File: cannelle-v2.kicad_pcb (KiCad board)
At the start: 2 copper layers, 62 parts, among them P1 USB_OTG, U6 ICE40HX1K

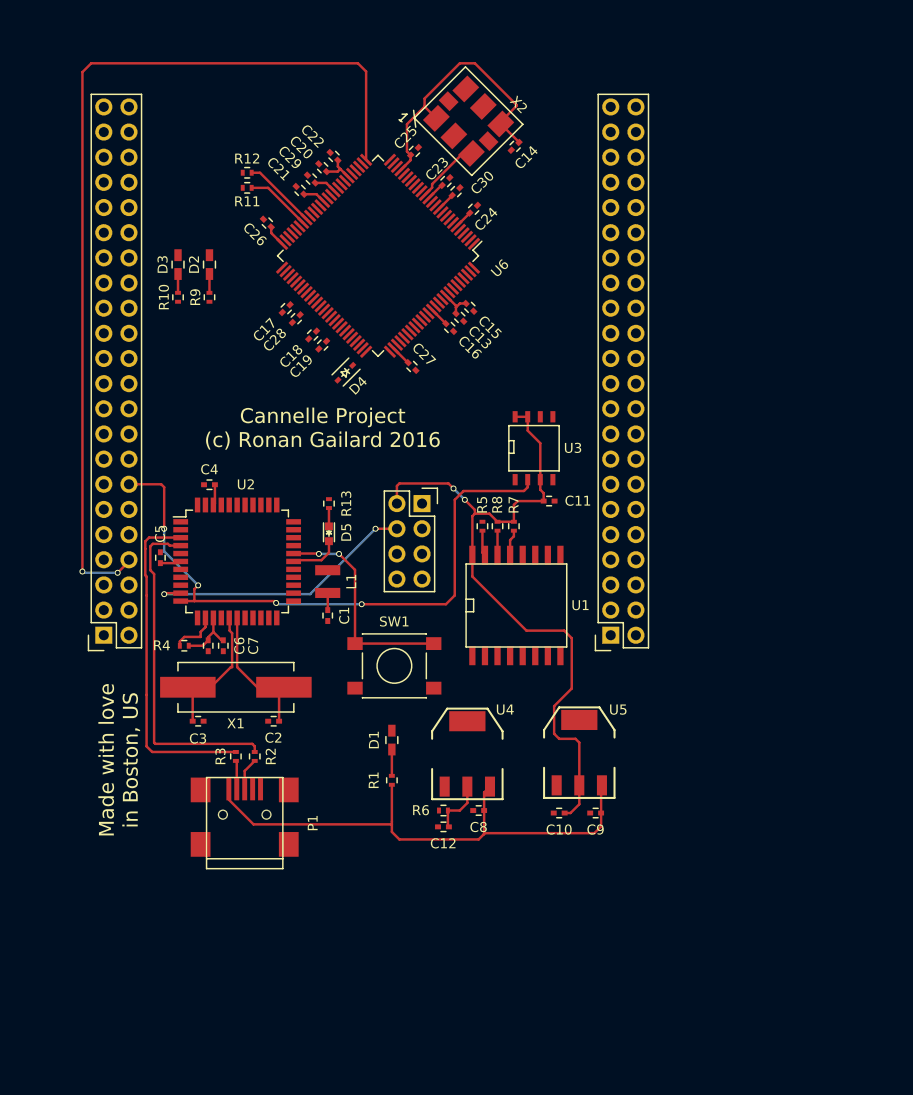
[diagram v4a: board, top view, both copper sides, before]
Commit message: Change in PCB with new connections
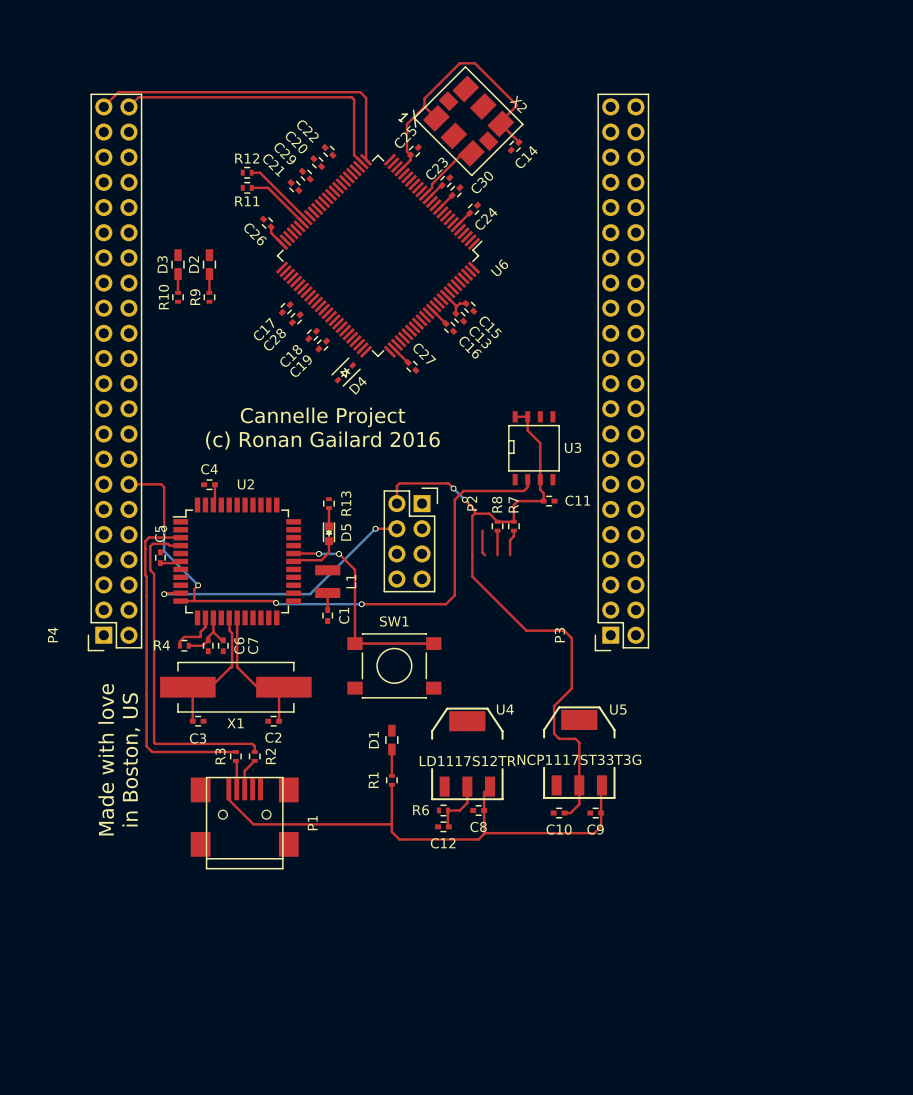
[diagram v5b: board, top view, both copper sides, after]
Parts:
- removed R5: , Resistors_SMD:R_0402
- removed U1: , SMD_Packages:SO-16-L
- C1, C4, C5: value (none) -> 1u
- C10, C11, C12, C13, C14, C15, C16, C17, C18, C19, C20, C21, C22, C23, C24, C25, C26, C27, C28, C29, C30, C6, C7, C8, C9: value (none) -> 100nF
- C2, C3: value (none) -> 22p
- D1, D2, D3, D5: value (none) -> LED
- D4: value (none) -> D_Schottky
- L1: value (none) -> 10uH
- P2: renamed from ?; value (none) -> CONN_02X04
- P3, P4: renamed from ?; value (none) -> CONN_02X22
- R1: value (none) -> 370
- R10, R12, R9: value (none) -> 2.2k
- R11, R4, R7, R8: value (none) -> 10k
- R13, R2, R3: value (none) -> 22
- R6: value (none) -> 120
- SW1: value (none) -> SW_PUSH
- U2: value (none) -> ATMEGA16U4-A
- U3: value (none) -> SST25VF020B
- U4: value (none) -> LD1117S12TR
- U5: value (none) -> NCP1117ST33T3G
- U6: value ICE40HX1K -> ICE40HX1K-VQ100
- X1: value (none) -> 8MHz
- X2: value (none) -> IQXO/7X
- moved C20 0.72 mm to (139.6, 50.3)
- moved C22 0.72 mm to (140.7, 49.1)
- moved C21 0.63 mm to (137.3, 52.7)
- moved C29 0.63 mm to (138.4, 51.6)
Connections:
- net Net-(P3-Pad16) renamed /FPGA/P3_16
- D2 pad 2: Net-(D2-Pad2) -> /FPGA/P4_43
- D3 pad 2: Net-(D3-Pad2) -> /FPGA/P4_44
- P1 pad 4: Net-(P1-Pad4) -> (no net)
- P2 pad 1: /AVR_MISO -> (no net)
- P2 pad 3: /AVR_SCK -> (no net)
- P2 pad 4: /AVR_MOSI -> (no net)
- P2 pad 8: Net-(P2-Pad8) -> (no net)
- P3 pad 1: GND -> /MISO
- P3 pad 10: Net-(P3-Pad10) -> /FPGA/P3_10
- P3 pad 11: /FPGA/GPIO_3 -> /FPGA/P3_11
- P3 pad 12: Net-(P3-Pad12) -> /FPGA/P3_12
- P3 pad 13: Net-(D3-Pad2) -> /FPGA/P3_13
- P3 pad 14: Net-(P3-Pad14) -> /FPGA/P3_14
- P3 pad 15: Net-(D2-Pad2) -> /FPGA/P3_15
- P3 pad 17: Net-(P3-Pad17) -> /FPGA/P3_17
- P3 pad 18: Net-(P3-Pad18) -> /FPGA/P3_18
- P3 pad 19: Net-(P3-Pad19) -> /FPGA/P3_19
- P3 pad 2: Net-(P3-Pad2) -> +5V
- P3 pad 20: Net-(P3-Pad20) -> /FPGA/P3_20
- P3 pad 21: Net-(P3-Pad21) -> /FPGA/P3_21
- P3 pad 22: Net-(P3-Pad22) -> /FPGA/P3_22
- P3 pad 23: Net-(P3-Pad23) -> /FPGA/P3_23
- P3 pad 24: Net-(P3-Pad24) -> /FPGA/P3_24
- P3 pad 25: Net-(P3-Pad25) -> /FPGA/P3_25
- P3 pad 26: Net-(P3-Pad26) -> /FPGA/P3_26
- P3 pad 27: Net-(P3-Pad27) -> /FPGA/P3_27
- P3 pad 28: Net-(P3-Pad28) -> /FPGA/P3_28
- P3 pad 29: Net-(P3-Pad29) -> /FPGA/P3_29
- P3 pad 3: +5V -> /MOSI
- P3 pad 30: Net-(P3-Pad30) -> /FPGA/P3_30
- P3 pad 31: Net-(P3-Pad31) -> /FPGA/P3_31
- P3 pad 32: Net-(P3-Pad32) -> /FPGA/P3_32
- P3 pad 33: Net-(P3-Pad33) -> /FPGA/P3_33
- P3 pad 34: Net-(P3-Pad34) -> /FPGA/P3_34
- P3 pad 35: Net-(P3-Pad35) -> /FPGA/P3_35
- P3 pad 36: Net-(P3-Pad36) -> /FPGA/P3_36
- P3 pad 37: Net-(P3-Pad37) -> /FPGA/P3_37
- P3 pad 38: Net-(P3-Pad38) -> /FPGA/P3_38
- P3 pad 39: Net-(P3-Pad39) -> /FPGA/P3_39
- P3 pad 4: Net-(P3-Pad4) -> +3V3
- P3 pad 40: Net-(P3-Pad40) -> /FPGA/P3_40
- P3 pad 41: Net-(P3-Pad41) -> /FPGA/P3_41
- P3 pad 42: Net-(P3-Pad42) -> /FPGA/P3_42
- P3 pad 43: Net-(P3-Pad43) -> /FPGA/P3_43
- P3 pad 44: Net-(P3-Pad44) -> /FPGA/P3_44
- P3 pad 5: +3V3 -> /SCK
- P3 pad 6: Net-(P3-Pad6) -> +1V2
- P3 pad 7: +1V2 -> /FPGA_SS
- P3 pad 8: Net-(P3-Pad8) -> GND
- P3 pad 9: Net-(P3-Pad9) -> /FPGA/P3_09
- P4 pad 1: Net-(P4-Pad1) -> /FPGA/DONE
- P4 pad 10: /AVR_TX -> GND
- P4 pad 11: Net-(P4-Pad11) -> /ADC3
- P4 pad 12: /AVR_RX -> (no net)
- P4 pad 13: Net-(P4-Pad13) -> /AVR_RX
- P4 pad 14: /MISO -> (no net)
- P4 pad 15: Net-(P4-Pad15) -> /FPGA/P4_15
- P4 pad 16: /FPGA_MOSI -> /AVR_TX
- P4 pad 17: Net-(P4-Pad17) -> /FPGA/P4_17
- P4 pad 18: /FPGA_SCK -> /FPGA/P4_18
- P4 pad 19: Net-(P4-Pad19) -> /FPGA/P4_19
- P4 pad 2: Net-(P4-Pad2) -> /ADC4
- P4 pad 20: /FPGA_SS -> /FPGA/P4_20
- P4 pad 21: Net-(P4-Pad21) -> /FPGA/P4_21
- P4 pad 22: /FPGA/SYSCLK -> /FPGA/P4_22
- P4 pad 23: Net-(P4-Pad23) -> /FPGA/P4_23
- P4 pad 24: /FPGA/DONE -> /FPGA/P4_24
- P4 pad 25: Net-(P4-Pad25) -> /FPGA/P4_25
- P4 pad 26: /FPGA/ICE40_RESET -> /FPGA/P4_26
- P4 pad 27: Net-(P4-Pad27) -> /FPGA/P4_27
- P4 pad 28: /ADC0 -> /FPGA/P4_28
- P4 pad 29: Net-(P4-Pad29) -> /FPGA/P4_29
- P4 pad 3: Net-(P4-Pad3) -> /FPGA/ICE40_RESET
- P4 pad 30: /ADC1 -> /FPGA/P4_30
- P4 pad 31: Net-(P4-Pad31) -> /FPGA/P4_31
- P4 pad 32: /ADC2 -> /FPGA/P4_32
- P4 pad 33: Net-(P4-Pad33) -> /FPGA/P4_33
- P4 pad 34: /ADC3 -> /FPGA/P4_34
- P4 pad 35: Net-(P4-Pad35) -> /FPGA/P4_35
- P4 pad 36: /ADC4 -> /FPGA/P4_36
- P4 pad 37: Net-(P4-Pad37) -> /FPGA/P4_37
- P4 pad 38: /ADC5 -> /FPGA/P4_38
- P4 pad 39: Net-(P4-Pad39) -> /FPGA/P4_39
- P4 pad 4: Net-(P4-Pad4) -> /ADC5
- P4 pad 40: /ADC6 -> /FPGA/P4_40
- P4 pad 41: Net-(P4-Pad41) -> /FPGA/P4_41
- P4 pad 42: /ADC7 -> /FPGA/P4_42
- P4 pad 43: Net-(P4-Pad43) -> /FPGA/P4_43
- P4 pad 44: GND -> /FPGA/P4_44
- P4 pad 5: Net-(P4-Pad5) -> /ADC0
- P4 pad 6: Net-(P4-Pad6) -> /ADC6
- P4 pad 7: Net-(P4-Pad7) -> /ADC1
- P4 pad 8: Net-(P4-Pad8) -> /ADC7
- P4 pad 9: Net-(P4-Pad9) -> /ADC2
- R8 pad 2: /AVR_SS -> (no net)
- U2 pad 1: Net-(U2-Pad1) -> (no net)
- U2 pad 10: /AVR_MOSI -> /MOSI
- U2 pad 12: Net-(U2-Pad12) -> (no net)
- U2 pad 15: Net-(U2-Pad15) -> (no net)
- U2 pad 18: Net-(U2-Pad18) -> (no net)
- U2 pad 19: Net-(U2-Pad19) -> (no net)
- U2 pad 2: Net-(U2-Pad2) -> (no net)
- U2 pad 22: Net-(U2-Pad22) -> (no net)
- U2 pad 23: Net-(U2-Pad23) -> (no net)
- U2 pad 25: Net-(U2-Pad25) -> (no net)
- U2 pad 31: Net-(U2-Pad31) -> /FPGA_SS
- U2 pad 32: Net-(U2-Pad32) -> /SS_FLASH
- U2 pad 33: Net-(U2-Pad33) -> (no net)
- U2 pad 35: Net-(U2-Pad35) -> (no net)
- U2 pad 8: /AVR_SS -> (no net)
- U2 pad 9: /AVR_SCK -> /SCK
- U3 pad 1: /CS_FLASH -> /SS_FLASH
- U3 pad 5: /FLASH_MOSI -> /MOSI
- U3 pad 6: /FLASH_SCK -> /SCK
- U6 pad 1: /AVR_TX -> /FPGA/P3_28
- U6 pad 10: Net-(P4-Pad27) -> /FPGA/P3_35
- U6 pad 100: Net-(P3-Pad38) -> /FPGA/P3_27
- U6 pad 12: Net-(P4-Pad29) -> /FPGA/P3_36
- U6 pad 13: /FPGA/GPIO_3 -> /FPGA/P3_37
- U6 pad 16: Net-(P4-Pad31) -> /FPGA/P3_38
- U6 pad 18: Net-(P4-Pad33) -> /FPGA/P3_39
- U6 pad 19: Net-(P4-Pad35) -> /FPGA/P3_40
- U6 pad 2: /AVR_RX -> /FPGA/P3_29
- U6 pad 20: Net-(P4-Pad37) -> /FPGA/P3_41
- U6 pad 21: Net-(P4-Pad39) -> /FPGA/P3_42
- U6 pad 24: Net-(P4-Pad41) -> /FPGA/P3_43
- U6 pad 25: Net-(P4-Pad43) -> /FPGA/P3_44
- U6 pad 26: Net-(P4-Pad8) -> /FPGA/P4_43
- U6 pad 27: Net-(P4-Pad6) -> /FPGA/P4_44
- U6 pad 28: Net-(P4-Pad4) -> /FPGA/P4_41
- U6 pad 29: Net-(P4-Pad2) -> /FPGA/P4_42
- U6 pad 3: Net-(P4-Pad17) -> /FPGA/P3_30
- U6 pad 30: Net-(P4-Pad1) -> /FPGA/P4_39
- U6 pad 33: Net-(P4-Pad3) -> /FPGA/P4_40
- U6 pad 34: Net-(P4-Pad5) -> /FPGA/P4_37
- U6 pad 36: Net-(P4-Pad7) -> /FPGA/P4_38
- U6 pad 37: Net-(P4-Pad9) -> /FPGA/P4_35
- U6 pad 4: Net-(P4-Pad19) -> /FPGA/P3_31
- U6 pad 40: Net-(P4-Pad11) -> /FPGA/P4_36
- U6 pad 41: Net-(P4-Pad13) -> /FPGA/P4_33
- U6 pad 42: Net-(P4-Pad15) -> /FPGA/P4_34
- U6 pad 46: /FPGA_MOSI -> /MOSI
- U6 pad 48: /FPGA_SCK -> /SCK
- U6 pad 51: Net-(P3-Pad40) -> /FPGA/P4_31
- U6 pad 52: Net-(P3-Pad42) -> /FPGA/P4_32
- U6 pad 53: Net-(P3-Pad44) -> /FPGA/P4_29
- U6 pad 54: Net-(P3-Pad43) -> /FPGA/P4_30
- U6 pad 56: Net-(P3-Pad41) -> /FPGA/P4_27
- U6 pad 57: Net-(P3-Pad39) -> /FPGA/P4_28
- U6 pad 59: Net-(P3-Pad37) -> /FPGA/P4_25
- U6 pad 60: Net-(P3-Pad35) -> /FPGA/P4_26
- U6 pad 62: Net-(P3-Pad33) -> /FPGA/P4_23
- U6 pad 63: Net-(P3-Pad31) -> /FPGA/P4_24
- U6 pad 64: Net-(P3-Pad29) -> /FPGA/P4_21
- U6 pad 65: Net-(P3-Pad27) -> /FPGA/P4_22
- U6 pad 66: Net-(P3-Pad25) -> /FPGA/P4_19
- U6 pad 68: Net-(P3-Pad23) -> /FPGA/P4_20
- U6 pad 69: Net-(P3-Pad21) -> /FPGA/P4_17
- U6 pad 7: Net-(P4-Pad21) -> /FPGA/P3_32
- U6 pad 71: Net-(P3-Pad19) -> /FPGA/P4_18
- U6 pad 72: Net-(P3-Pad17) -> /FPGA/P4_15
- U6 pad 73: Net-(D2-Pad2) -> /AVR_TX
- U6 pad 74: Net-(D3-Pad2) -> /AVR_RX
- U6 pad 76: Net-(U6-Pad76) -> (no net)
- U6 pad 78: Net-(P3-Pad2) -> /FPGA/P3_09
- U6 pad 79: Net-(P3-Pad4) -> /FPGA/P3_10
- U6 pad 8: Net-(P4-Pad23) -> /FPGA/P3_33
- U6 pad 80: Net-(P3-Pad6) -> /FPGA/P3_11
- U6 pad 81: Net-(P3-Pad8) -> /FPGA/P3_12
- U6 pad 82: Net-(P3-Pad10) -> /FPGA/P3_13
- U6 pad 83: Net-(P3-Pad12) -> /FPGA/P3_14
- U6 pad 85: Net-(P3-Pad14) -> /FPGA/P3_15
- U6 pad 87: Net-(P3-Pad18) -> /FPGA/P3_17
- U6 pad 89: Net-(P3-Pad20) -> /FPGA/P3_18
- U6 pad 9: Net-(P4-Pad25) -> /FPGA/P3_34
- U6 pad 90: Net-(P3-Pad22) -> /FPGA/P3_19
- U6 pad 91: Net-(P3-Pad24) -> /FPGA/P3_20
- U6 pad 93: Net-(P3-Pad26) -> /FPGA/P3_21
- U6 pad 94: Net-(P3-Pad28) -> /FPGA/P3_22
- U6 pad 95: Net-(P3-Pad30) -> /FPGA/P3_23
- U6 pad 96: Net-(P3-Pad32) -> /FPGA/P3_24
- U6 pad 97: Net-(P3-Pad34) -> /FPGA/P3_25
- U6 pad 99: Net-(P3-Pad36) -> /FPGA/P3_26
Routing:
- net Net-(P4-Pad8): track 94.1 -> 0.00 mm, vias 2 -> 0
- net /FPGA/P4_43: track 0.00 -> 33.6 mm
- net /FPGA/P4_44: track 0.00 -> 30.0 mm
- net /MOSI: track 0.00 -> 27.9 mm, vias 0 -> 2
- net /AVR_MOSI: track 27.9 -> 0.00 mm, vias 2 -> 0
- net +3V3: track 124.8 -> 118.7 mm
- net (no net): track 0.00 -> 5.05 mm
- net Net-(R5-Pad1): track 2.58 -> 0.00 mm
- net /AVR_SS: track 2.47 -> 0.00 mm
- net +1V2: track 11.9 -> 9.61 mm

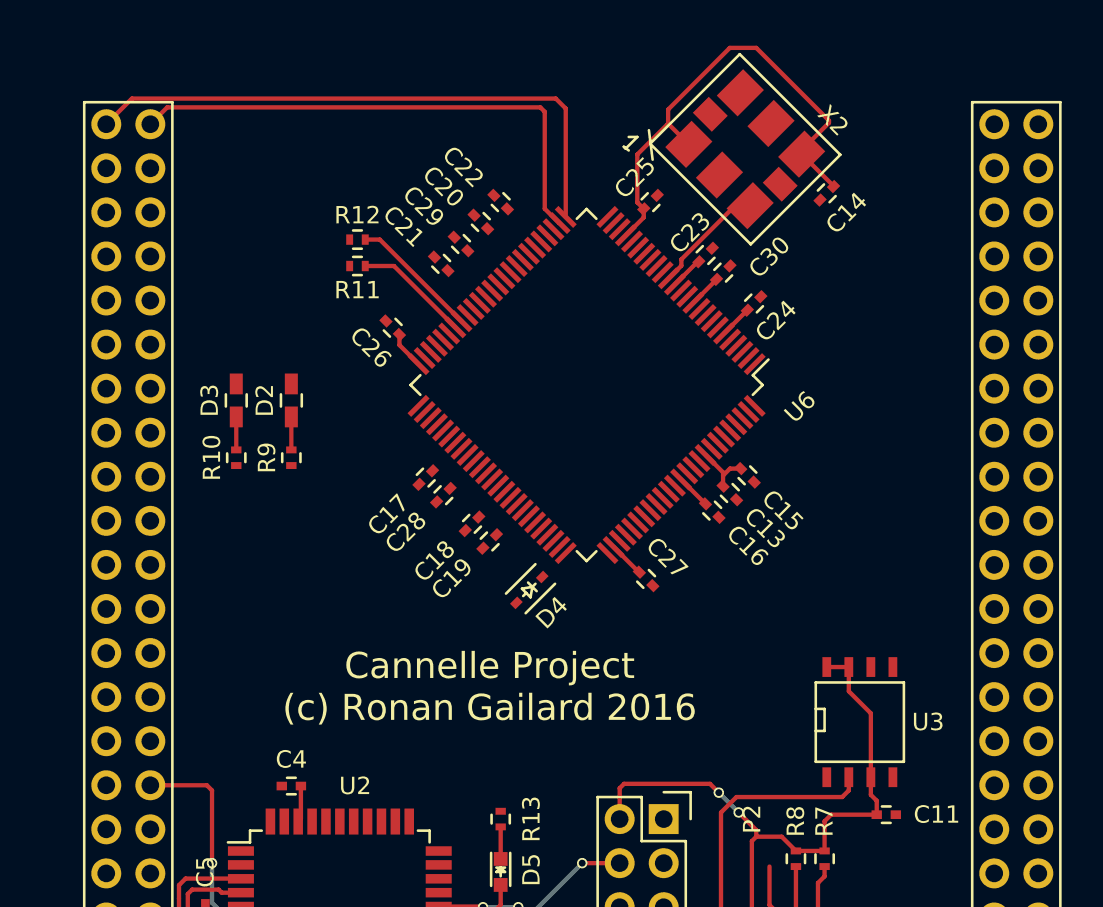
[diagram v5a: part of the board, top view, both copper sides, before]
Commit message: Add more wires on PCB
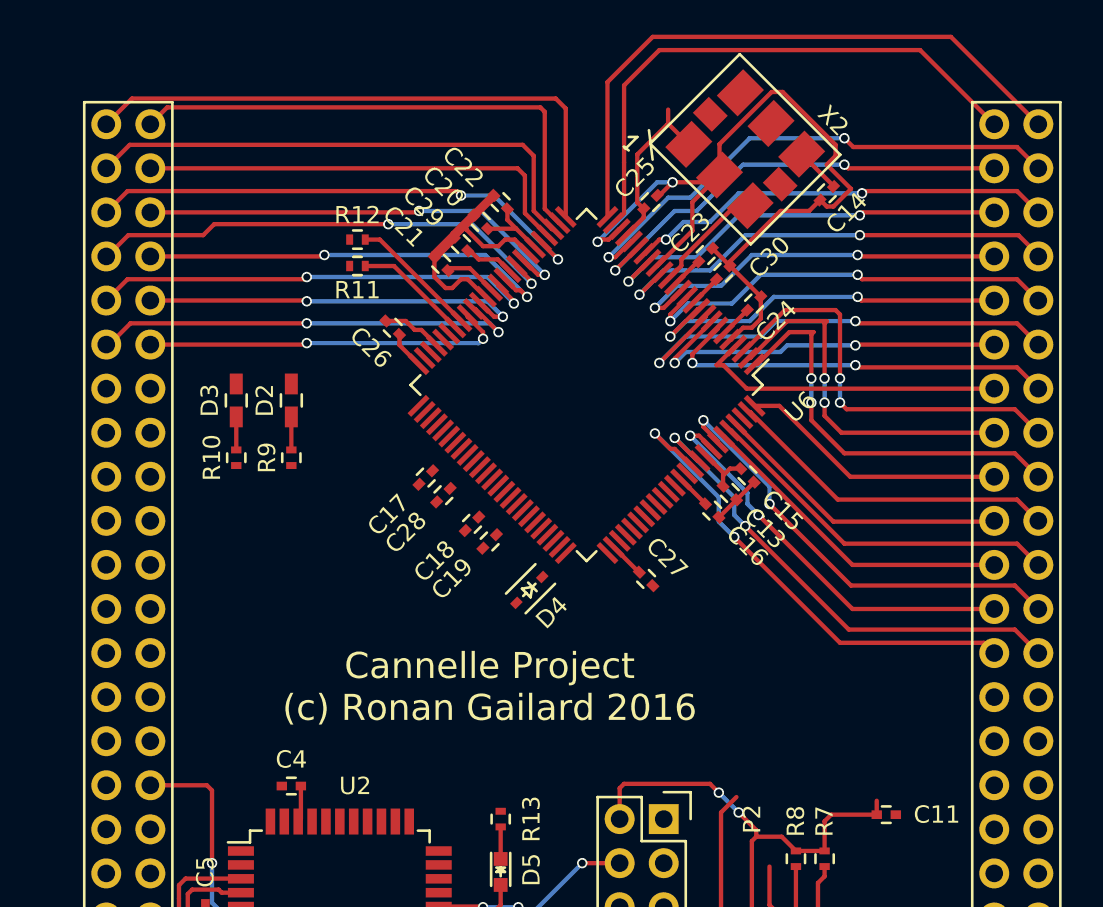
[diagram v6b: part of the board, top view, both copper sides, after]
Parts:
- removed U3: SST25VF020B, SMD_Packages:SOIC-8-N
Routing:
- net GND: track 0.00 -> 74.5 mm, vias 0 -> 2
- net /FPGA/P3_44: track 0.00 -> 35.8 mm
- net /FPGA/P3_43: track 0.00 -> 32.2 mm
- net /FPGA/P4_41: track 0.00 -> 30.2 mm
- net /FPGA/P3_42: track 0.00 -> 30.0 mm, vias 0 -> 2
- net /FPGA/P4_39: track 0.00 -> 29.6 mm, vias 0 -> 2
- net /FPGA/P3_20: track 0.00 -> 28.7 mm, vias 0 -> 2
- net /FPGA/P3_19: track 0.00 -> 28.6 mm, vias 0 -> 2
- net /FPGA/P4_37: track 0.00 -> 28.1 mm, vias 0 -> 2
- net /FPGA/P3_34: track 0.00 -> 27.3 mm, vias 0 -> 2
- net /FPGA/P3_38: track 0.00 -> 26.8 mm, vias 0 -> 2
- net /FPGA/P3_41: track 0.00 -> 26.3 mm, vias 0 -> 2
- net /FPGA/P4_35: track 0.00 -> 26.2 mm, vias 0 -> 2
- net /FPGA/P3_22: track 0.00 -> 26.0 mm, vias 0 -> 2
- net /FPGA/P4_40: track 0.00 -> 25.9 mm, vias 0 -> 2
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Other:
- net class Default: clearance 0.2 -> 0.15
- rule trace_clearance: 0.2 -> 0.15

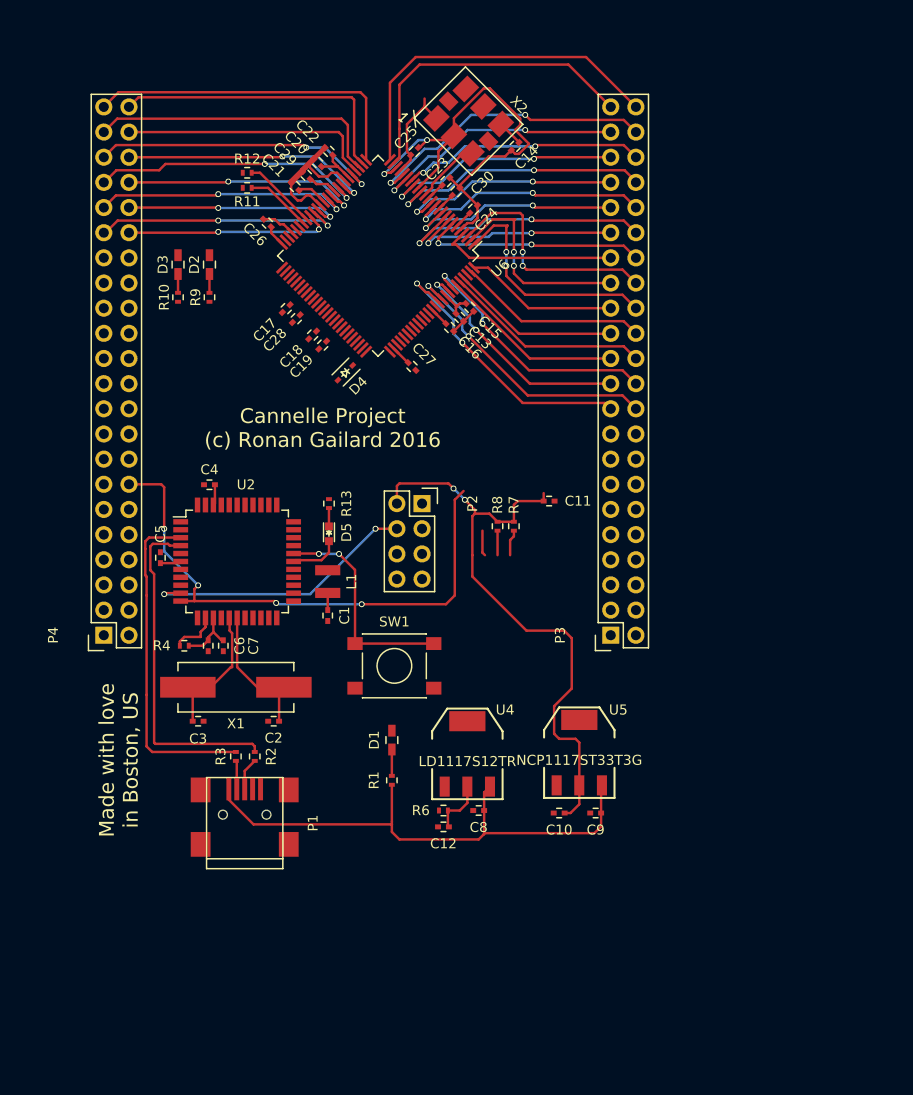
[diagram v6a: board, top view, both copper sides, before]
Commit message: Connect more on PCB and modify the schem a bit
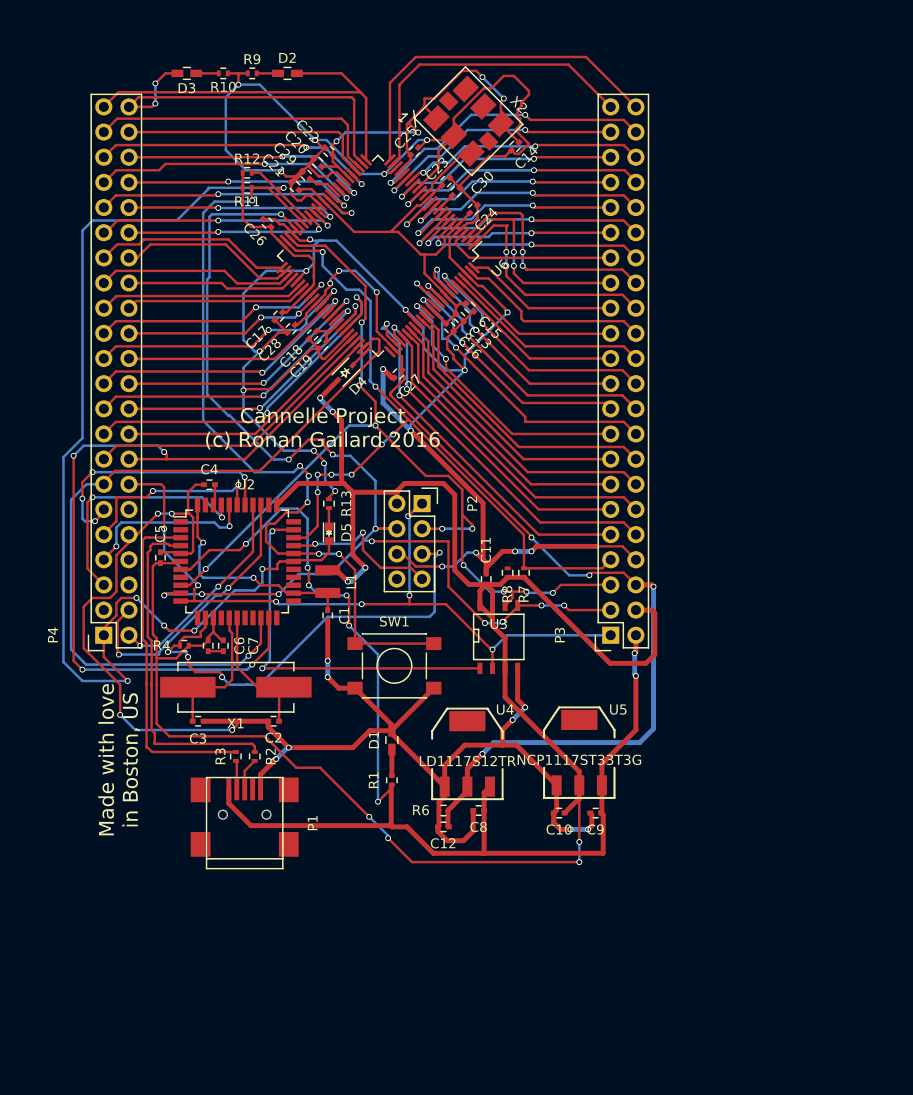
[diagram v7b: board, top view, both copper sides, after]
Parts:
- added U3: SST25VF020B, SMD_Packages:SOIC-8-N, F.Cu at (157.9, 98.2)
- moved R10 23.1 mm to (130.0, 41.3), turned to 180 degrees
- moved R9 23.0 mm to (133.0, 41.3), turned to 0 degrees
- moved D2 20.8 mm to (136.5, 41.3), turned to 0 degrees
- moved D3 19.3 mm to (126.4, 41.3), turned to 180 degrees
- moved C11 10.1 mm to (156.6, 92.3), turned to 90 degrees
- moved R7 4.81 mm to (160.4, 91.7), turned to 90 degrees
- moved R8 4.81 mm to (158.8, 91.7), turned to 90 degrees
- moved C27 1.59 mm to (147.7, 71.6), turned to 225 degrees
- moved C28 1.14 mm to (136.9, 67.1)
- moved C17 1.08 mm to (135.6, 65.8)
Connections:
- net /ADC0 renamed /FPGA/ADC0
- net /ADC1 renamed /FPGA/ADC1
- net /ADC2 renamed /FPGA/ADC2
- net /ADC3 renamed /FPGA/ADC3
- net /ADC4 renamed /FPGA/ADC4
- net /ADC5 renamed /FPGA/ADC5
- net /AVR_RX renamed /FPGA/AVR_RX
- net /AVR_TX renamed /FPGA/AVR_TX
- net /FPGA_SS renamed /FPGA/ICE40_SS
- P1 pad 4: (no net) -> Net-(P1-Pad4)
- P2 pad 1: (no net) -> /FPGA/ICE40_SDO
- P2 pad 3: (no net) -> /FPGA/ICE40_SCK
- P2 pad 4: (no net) -> /FPGA/ICE40_SDI
- P2 pad 8: (no net) -> Net-(P2-Pad8)
- P3 pad 1: /MISO -> /FPGA/ICE40_SDO
- P3 pad 3: /MOSI -> /FPGA/ICE40_SDI
- P3 pad 5: /SCK -> /FPGA/ICE40_SCK
- P4 pad 12: (no net) -> /FPGA/P4_12
- P4 pad 14: (no net) -> /FPGA/P4_14
- P4 pad 6: /ADC6 -> /FPGA/ADC6
- P4 pad 8: /ADC7 -> /FPGA/ADC7
- R8 pad 2: (no net) -> /AVR_SS
- U2 pad 1: (no net) -> Net-(U2-Pad1)
- U2 pad 10: /MOSI -> /FPGA/ICE40_SDI
- U2 pad 11: /MISO -> /FPGA/ICE40_SDO
- U2 pad 12: (no net) -> Net-(U2-Pad12)
- U2 pad 15: (no net) -> Net-(U2-Pad15)
- U2 pad 18: (no net) -> Net-(U2-Pad18)
- U2 pad 19: (no net) -> Net-(U2-Pad19)
- U2 pad 2: (no net) -> Net-(U2-Pad2)
- U2 pad 22: (no net) -> Net-(U2-Pad22)
- U2 pad 23: (no net) -> Net-(U2-Pad23)
- U2 pad 25: (no net) -> Net-(U2-Pad25)
- U2 pad 33: (no net) -> Net-(U2-Pad33)
- U2 pad 35: (no net) -> Net-(U2-Pad35)
- U2 pad 8: (no net) -> /SS
- U2 pad 9: /SCK -> /FPGA/ICE40_SCK
- U6 pad 45: /MISO -> /FPGA/ICE40_SDO
- U6 pad 46: /MOSI -> /FPGA/ICE40_SDI
- U6 pad 48: /SCK -> /FPGA/ICE40_SCK
- U6 pad 76: (no net) -> Net-(U6-Pad76)
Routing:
- net GND: track 74.5 -> 445.6 mm, vias 2 -> 33
- net +3V3: track 102.0 -> 310.0 mm, vias 2 -> 12
- net /FPGA/ICE40_SDI: track 0.00 -> 117.4 mm, vias 0 -> 12
- net /FPGA/DONE: track 12.6 -> 120.1 mm, vias 0 -> 6
- net /FPGA/ICE40_SCK: track 0.00 -> 95.4 mm, vias 0 -> 10
- net +1V2: track 12.6 -> 105.7 mm, vias 0 -> 7
- net /FPGA/AVR_TX: track 0.00 -> 83.4 mm, vias 0 -> 4
- net /FPGA/AVR_RX: track 0.00 -> 79.1 mm, vias 0 -> 1
- net +5V: track 54.5 -> 128.7 mm, vias 0 -> 8
- net /FPGA/ICE40_SDO: track 0.00 -> 71.9 mm, vias 0 -> 7
- net /FPGA/ICE40_SS: track 2.63 -> 74.2 mm, vias 0 -> 8
- net /MISO: track 55.8 -> 0.00 mm, vias 4 -> 0
- net /FPGA/ICE40_RESET: track 28.9 -> 83.0 mm, vias 2 -> 6
- net /RST_AVR: track 4.85 -> 46.6 mm, vias 0 -> 4
- net /SS_FLASH: track 0.00 -> 38.4 mm, vias 0 -> 2
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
